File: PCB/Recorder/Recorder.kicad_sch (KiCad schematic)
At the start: 58 parts, among them J1 Reset, J3 TC2030-USB-NL-DS, J4 TF_PUSH, J5 USB-C-Socket-H, J6 Battery, Q1 CJ2301, SW1 SW_Push_DPDT, U1 ESP32-S3-MINI-1-N4R2, U2 TPS22916CNYFPR, U3 TP4054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

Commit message: needs work on case
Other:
- note added: "TODO Button finger press hole Split TF_PUSH so can do no finger on bigger cases Some sort of clip in case design"
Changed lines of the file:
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@@
+		)
+	)
+	(text "TODO\nButton finger press hole\nSplit TF_PUSH so can do no finger on bigger cases\nSome sort of clip in case design"
+		(exclude_from_sim no)
+		(at 20.066 196.596 0)
+		(effects
+			(font
+				(size 5.08 5.08)
+			)
+			(justify left)
 		)
 	)

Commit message: notes
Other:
- note added: "TODO Button finger press hole Split TF_PUSH so can do no finger on bigger cases Some sort of clip in case design Covred LED holes"
- note removed: "TODO Button finger press hole Split TF_PUSH so can do no finger on bigger cases Some sort of clip in case design"
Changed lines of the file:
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@@
 		)
 	)
-	(text "TODO\nButton finger press hole\nSplit TF_PUSH so can do no finger on bigger cases\nSome sort of clip in case design"
+	(text "TODO\nButton finger press hole\nSplit TF_PUSH so can do no finger on bigger cases\nSome sort of clip in case design\nCovred LED holes"
 		(exclude_from_sim no)
 		(at 20.066 196.596 0)

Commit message: Library update
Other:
- note added: "TODO Button finger press hole Block on mic for sideways Move SD finger to lowest level of insert Split TF_PUSH so can do no finger on bigger cases Some sort of clip in case design Covred LED holes"
- note removed: "TODO Button finger press hole Split TF_PUSH so can do no finger on bigger cases Some sort of clip in case design Covred LED holes"
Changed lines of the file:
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@@
 		)
 	)
-	(text "TODO\nButton finger press hole\nSplit TF_PUSH so can do no finger on bigger cases\nSome sort of clip in case design\nCovred LED holes"
+	(text "TODO\nButton finger press hole\nBlock on mic for sideways\nMove SD finger to lowest level of insert\nSplit TF_PUSH so can do no finger on bigger cases\nSome sort of clip in case design\nCovred LED holes"
 		(exclude_from_sim no)
 		(at 20.066 196.596 0)

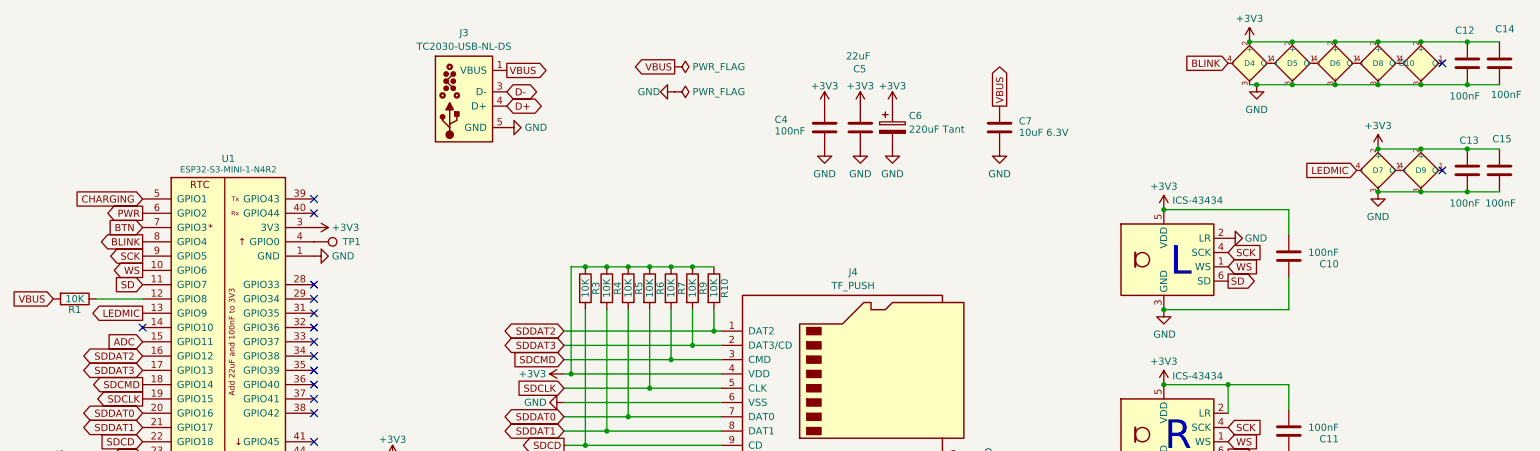
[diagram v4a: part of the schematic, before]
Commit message: New LEDs
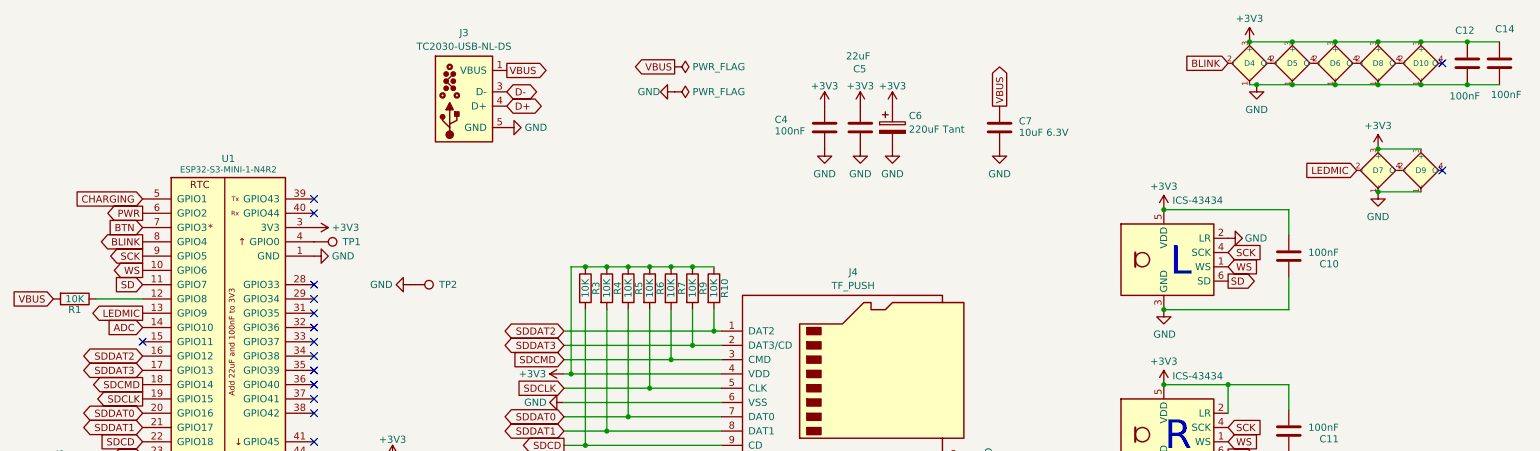
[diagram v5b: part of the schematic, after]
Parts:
- removed C13, C15: 100nF, RevK:C_0201, symbol Device:C
- added TP2: TestPoint, RevK:PAD-2mm, symbol Connector:TestPoint
- D10, D4, D5, D6, D7, D8, D9: footprint RevK:SMD1010 -> RevK:SMD1615; symbol RevK:WS2812B-1mm -> RevK:WS2812B-1.5mm; MPN C5349953 -> C5349954
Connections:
- net +3V3: now also D10.3 (+), D4.3 (+), D5.3 (+), D6.3 (+), D7.3 (+), D8.3 (+), D9.3 (+); no longer D10.2 (+), D4.2 (+), D5.2 (+), D6.2 (+), D7.2 (+), D8.2 (+), D9.2 (+)
- net ADC: now also U1.14 (GPIO10); no longer U1.15 (GPIO11)
- net BLINK: now also D4.2 (I); no longer D4.4 (I)
- net GND: now also D10.1 (-), D4.1 (-), D5.1 (-), D6.1 (-), D7.1 (-), D8.1 (-), D9.1 (-), TP2.1; no longer D10.3 (-), D4.3 (-), D5.3 (-), D6.3 (-), D7.3 (-), D8.3 (-), D9.3 (-)
- net LEDMIC: now also D7.2 (I); no longer D7.4 (I)
- net at D10.4 (O): no longer D8.1 (O)
- net at D6.4 (O): now also D8.2 (I); no longer D5.1 (O)
- net at D5.4 (O): now also D6.2 (I); no longer D4.1 (O)
- net at D8.4 (O): now also D10.2 (I); no longer D6.1 (O)
- net at D9.4 (O): no longer D7.1 (O)
- new net: D4.4 (O), D5.2 (I)
- new net: D7.4 (O), D9.2 (I)
